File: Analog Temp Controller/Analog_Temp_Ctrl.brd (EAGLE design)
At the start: 100 x 59 mm, 110 parts, among them IC1 TL074D, IC10 74LVC1G125DCKR, IC3 LMV358MMX, IC4 ADA4522-2, Q1 TIP41C, T1 2N3904, T2 2N3906, U1 ADR01BRZ, U3 CJT1117-3.3-SOT223, U4 CJT1117-5.0-SOT223, U5 ATSAMD21G-A, Y1 32,768Khz_SMD

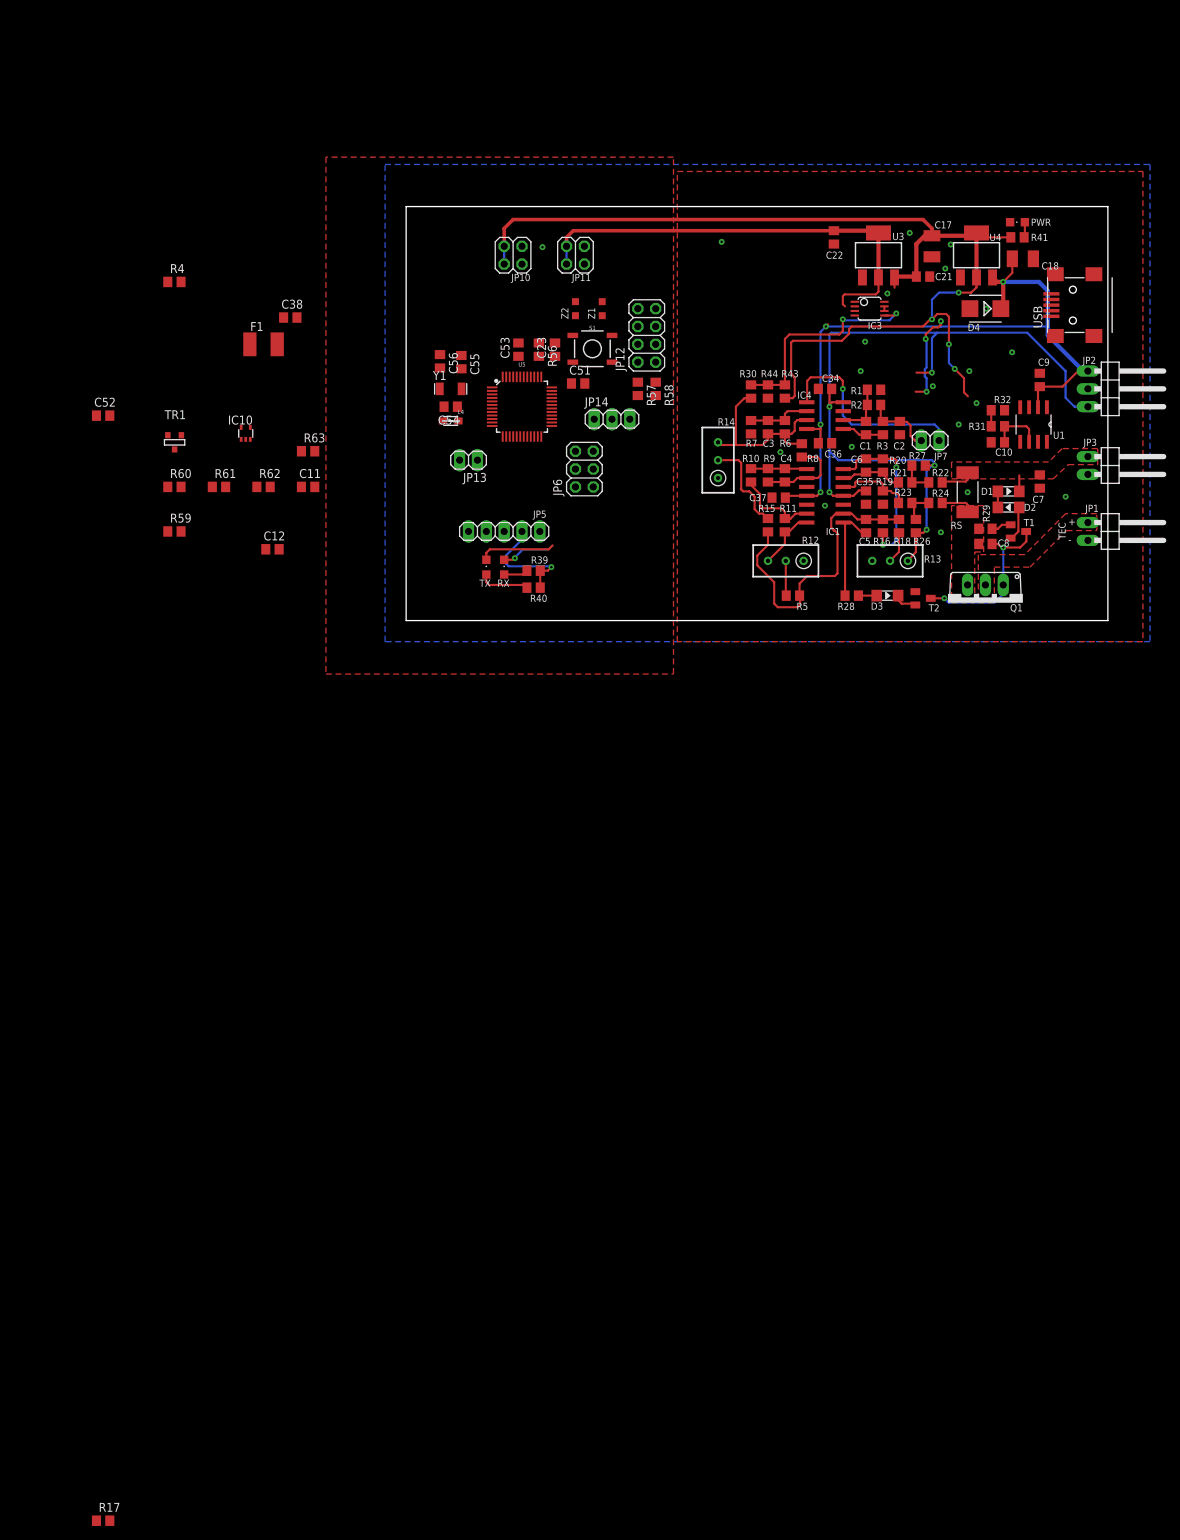
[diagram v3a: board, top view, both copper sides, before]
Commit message: Added a Controller for the Pfeiffer IKR/PKR Series Compact Gauges. Temp Ctrl WIP...
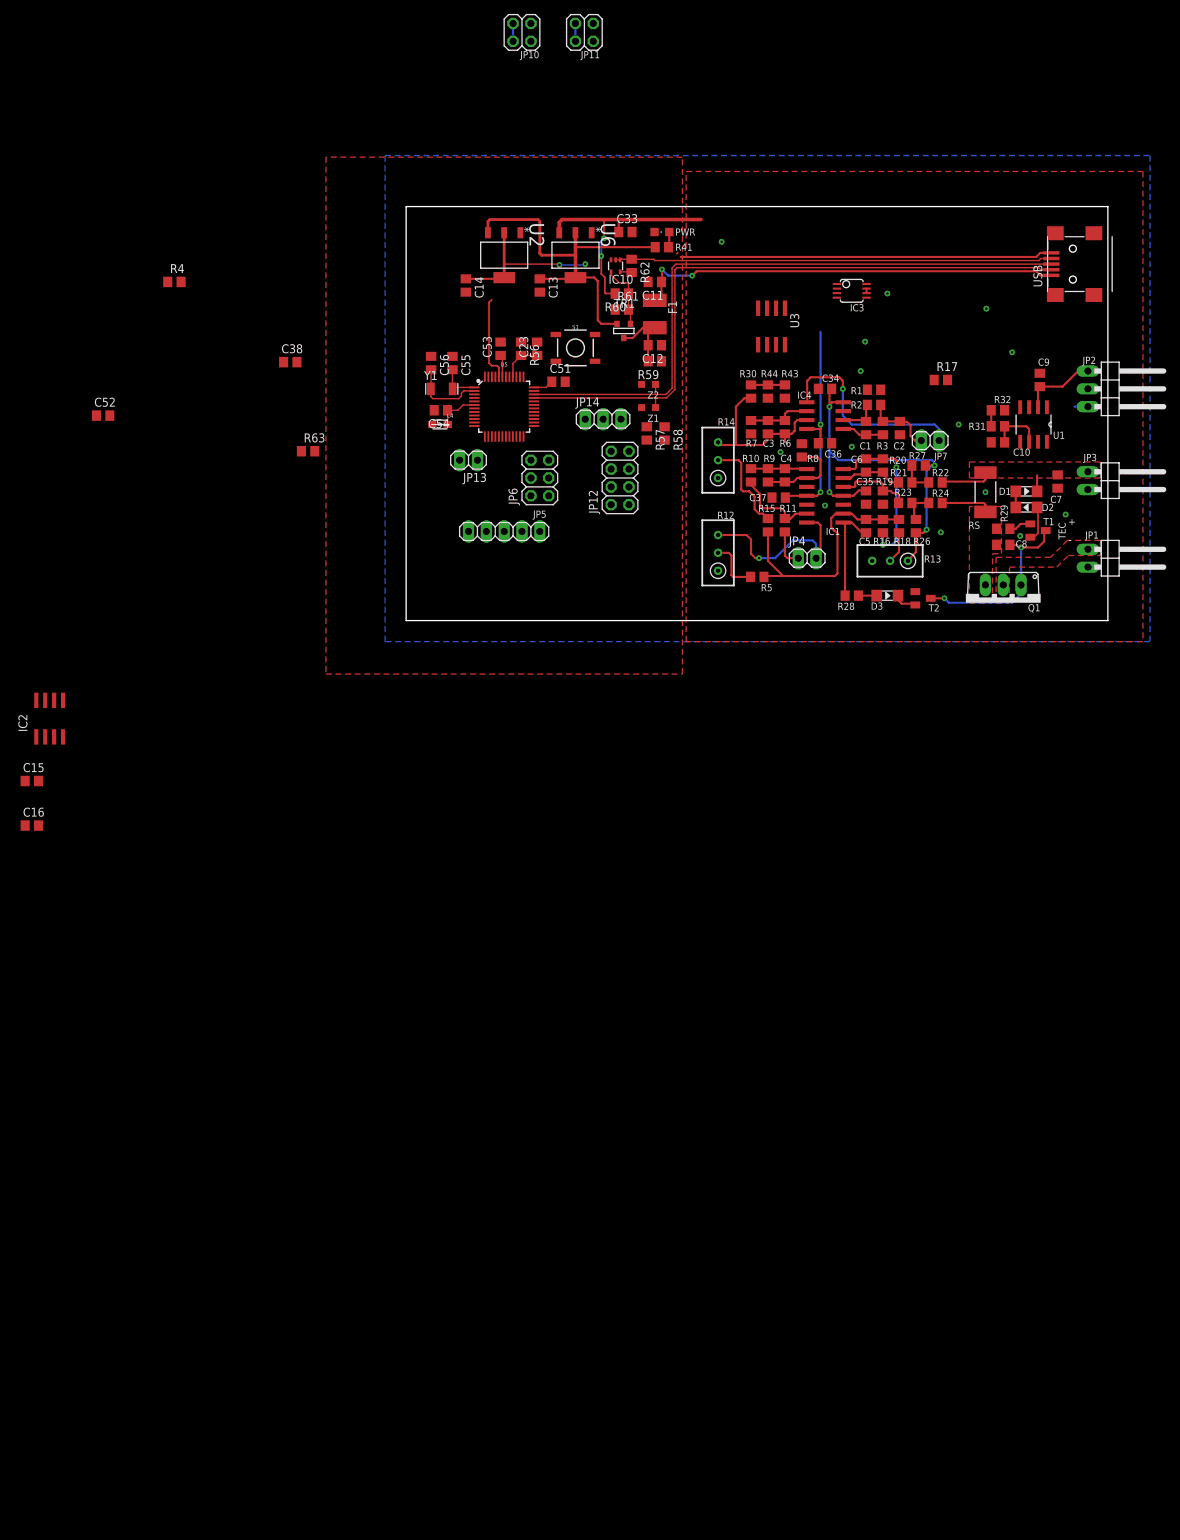
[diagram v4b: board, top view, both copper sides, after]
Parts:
- removed C17, C18: 10uF, rcl:SMC_B
- removed C21, C22: 1uF, rcl:C0805
- removed D4: (no value), diode:SMB
- removed R39, R40: 1K, rcl:R0805
- removed RX, TX: (no value), led:CHIPLED_0805
- removed U4: CJT1117-5.0-SOT223, Seeed-IC:SOT-223
- added C13, C14, C33: 10uF, rcl:C0805
- added C15, C16: 0.1uF, rcl:C0805
- added IC2: AD620R, analog-devices:SO8
- added JP4: (no value), pinhead:1X02
- added U2: LM1117IMP-3.3, NSC_By_element14_Batch_1.1:SOT230P696X180-4N
- added U6: LM1117IMP-5.0, NSC_By_element14_Batch_1.1:SOT230P696X180-4N
- U3: value CJT1117-3.3-SOT223 -> AD5541; device Seeed-IC:SOT-223 -> misc-ics:SOIC-8
- moved R17 201.7 mm to (76.2, 34.3)
- moved R59 72.6 mm to (35.4, 37.0), turned to 180 degrees
- moved R60 69.5 mm to (30.7, 46.6), turned to 180 degrees
- moved TR1 65.9 mm to (31.0, 41.3)
- moved R61 62.7 mm to (30.7, 44.3)
- moved C12 61.8 mm to (35.4, 39.2), turned to 180 degrees
- moved R62 61.2 mm to (32.1, 50.5), turned to 270 degrees
- moved IC10 57.9 mm to (29.8, 50.5), turned to 180 degrees
- moved C11 57.4 mm to (35.4, 48.3), turned to 180 degrees
- moved F1 55.9 mm to (35.4, 43.7), turned to 270 degrees
- moved PWR 50.7 mm to (36.4, 55.4)
- moved R41 50.7 mm to (36.4, 53.2)
- moved JP10 31.8 mm to (16.5, 83.8)
- moved JP11 31.8 mm to (25.4, 83.8)
- moved JP12 20.7 mm to (30.5, 20.3)
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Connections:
- removed net +12V: R60.2
- removed net CS_DAC: U5.24
- removed net MOSI_DAC: U5.22
- removed net N$42: R39.1, RX.A
- removed net N$48: R40.1, TX.A
- removed net RXLED: RX.C
- removed net SCK_DAC: U5.23
- removed net TXLED: TX.C
- new net DCLK: U3.5, U5.23
- new net DCS: U3.4, U5.24
- new net DDATA: U3.6, U5.22
- new net N$2: JP4.1, R11.2
- new net N$36: IC2.2, U3.1
- new net N$7: C3.1, IC2.3, IC4.7, R6.2
- net +15V: now also C15.2, C33.1, IC2.7, R60.2, U6.3; no longer C18.+, D4.C, U4.3
- net +3V3: now also C14.1, U2.2, U2.4
- net +5V: now also C13.1, U2.3, U6.2, U6.4; no longer C17.+, C21.1, R39.2, R40.2, U3.3, U4.2, U4.TER
- net -15V: now also C16.1, IC2.4
- net 3V3: no longer C22.1, U3.2, U3.TER
- net DGND: now also C13.2, C14.2, C33.2, PWR.C, U2.1, U3.7, U6.1
- net GND: now also C15.1, C16.2, IC2.5, U3.2; no longer C17.-, C18.-, C21.2, C22.2, D4.A, PWR.C, U3.1, U4.1
- net N$10: no longer C3.1, IC4.7, R6.2, R8.1
- net N$20: now also JP4.2; no longer R11.2
- net VREG: now also U3.3, U3.8
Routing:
- net +5V: track 172.6 -> 56.4 mm, vias 5 -> 0
- net TARGET_USB_N: track 0.00 -> 92.9 mm
- net TARGET_USB_P: track 0.00 -> 92.9 mm
- net USB_ID: track 0.00 -> 62.3 mm
- net XUSB: track 0.00 -> 61.8 mm, vias 0 -> 2
- net 3V3: track 64.1 -> 2.54 mm
- net -15V: track 118.6 -> 58.3 mm, vias 5 -> 4
- net DGND: track 0.00 -> 53.2 mm
- net +15V: track 122.9 -> 81.6 mm, vias 7 -> 4
- net +3V3: track 0.00 -> 40.3 mm, vias 0 -> 2
- net UGBIN: track 31.6 -> 4.83 mm, vias 2 -> 0
- net N$20: track 8.80 -> 26.9 mm, vias 0 -> 1
- net N$10: track 27.2 -> 15.7 mm
- net USBVCC: track 0.00 -> 11.0 mm
- net TXLED: track 10.9 -> 0.00 mm
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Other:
- board text added: "I EN"
- board text added: "INT GAIN"
- board text removed: "INTEGRAL GAIN"

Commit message: Added Pfeiffer G.auge Controller Schematics + FW
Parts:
- removed Z1, Z2: BRNCG0603MLC-05E, Arduino-M0-V1:PROTEZIONE_CT/CN0603
- added H1, H2, H3, H4: MOUNT-PAD-ROUND2.8, holes:2,8-PAD
- added JP8: JUMPER-SMT_2_NO_SILK, SparkFun-Jumpers:SMT-JUMPER_2_NO_SILK
- moved C15 33.8 mm to (-25.4, -3.81)
- moved C16 33.8 mm to (-25.4, -10.2)
- moved IC2 32.1 mm to (-24.1, 3.81)
- moved R63 29.3 mm to (-11.4, 53.3)
- moved C52 26.8 mm to (-16.5, 31.8)
- moved JP14 19.1 mm to (26.8, 9.65)
- moved USB 3.81 mm to (96.0, 47.0)
- moved C1 1.78 mm to (65.5, 29.2)
- moved C10 1.78 mm to (84.3, 27.2)
- moved C2 1.78 mm to (70.4, 29.2)
- moved C6 1.78 mm to (65.5, 23.9)
- moved D1 1.78 mm to (88.4, 20.2)
- moved R14 1.78 mm to (44.5, 24.6)
- moved R20 1.78 mm to (67.9, 23.9)
- moved R21 1.78 mm to (71.1, 21.5)
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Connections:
- net DGND: no longer Z1.2, Z2.2
- net GND: now also H1.B2,8, H2.B2,8, H3.B2,8, H4.B2,8
- net TARGET_USB_N: no longer Z1.1
- net TARGET_USB_P: no longer Z2.1
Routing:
- net PB10_S4_SPI_MOSI: track 0.00 -> 14.5 mm, vias 0 -> 1
- net PB11_S4_SPI_SCK: track 0.00 -> 9.94 mm
- net PB12_S4_SPI_MISO: track 0.00 -> 6.89 mm
- net RESET: track 0.00 -> 4.73 mm
- net +15V: track 81.6 -> 79.9 mm
- net XUSB: track 61.8 -> 63.4 mm
- net USB_ID: track 62.3 -> 63.7 mm
- net DGND: track 53.2 -> 54.3 mm
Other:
- board size 100 x 59 mm -> 100 x 60 mm
